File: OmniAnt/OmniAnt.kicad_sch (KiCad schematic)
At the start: 2 parts, among them J1 Conn_01x01_Pin

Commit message: First commit through KiCad
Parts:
- added BT1: Battery_Cell, symbol Device:Battery_Cell
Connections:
- net GND: now also BT1.2 (-)
- net at J1.1 (Pin_1), R1.1: now also BT1.1 (+)
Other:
- moved on the sheet: J1
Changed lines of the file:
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@@
 	(generator_version "9.0")
 	(paper "A4")
-	(wire
-		(pts
-			(xy 110.49 92.71) (xy 110.49 100.33)
+	(junction
+		(at 85.09 82.55)
+		(diameter 0)
+		(color 0 0 0 0)
+	)
+	(junction
+		(at 92.71 82.55)
+		(diameter 0)
+		(color 0 0 0 0)
+	)
+	(junction
+		(at 110.49 92.71)
+		(diameter 0)
+		(color 0 0 0 0)
+	)
+	(wire
+		(pts
+			(xy 92.71 91.44) (xy 92.71 92.71)
+		)
+		(stroke
+			(width 0)
+			(type default)
+		)
+	)
+	(wire
+		(pts
+			(xy 85.09 82.55) (xy 92.71 82.55)
+		)
+		(stroke
+			(width 0)
+			(type default)
+		)
+	)
+	(wire
+		(pts
+			(xy 82.55 82.55) (xy 85.09 82.55)
+		)
+		(stroke
+			(width 0)
+			(type default)
+		)
+	)
+	(wire
+		(pts
+			(xy 92.71 92.71) (xy 110.49 92.71)
+		)
+		(stroke
+			(width 0)
+			(type default)
+		)
+	)
+	(wire
+		(pts
+			(xy 92.71 83.82) (xy 92.71 82.55)
 		)
 		(stroke
@@
 	(wire
 		(pts
-			(xy 95.25 82.55) (xy 110.49 82.55)
-		)
-		(stroke
-			(width 0)
-			(type default)
-		)
-	)
-	(wire
-		(pts
-			(xy 110.49 100.33) (xy 111.76 100.33)
+			(xy 92.71 82.55) (xy 110.49 82.55)
+		)
+		(stroke
+			(width 0)
+			(type default)
+		)
+	)
+	(wire
+		(pts
+			(xy 110.49 92.71) (xy 110.49 102.87)
 		)
 		(stroke
@@
 	(symbol
 		(lib_id "Connector:Conn_01x01_Pin")
-		(at 90.17 82.55 0)
+		(at 80.01 82.55 0)
+		(unit 1)
+		(exclude_from_sim no)
+		(in_bom yes)
+		(on_board yes)
+		(dnp no)
+		(property "Reference" "J1"
+			(at 80.645 77.47 0)
+			(effects
+				(font
+					(size 1.27 1.27)
+				)
+			)
+		)
+		(property "Value" "Conn_01x01_Pin"
+			(at 79.502 76.454 0)
+			(effects
+				(font
+					(size 1.27 1.27)
+				)
+			)
+		)
+		(property "Footprint" ""
+			(at 80.01 82.55 0)
+			(effects
+				(font
+					(size 1.27 1.27)
+				)
+				(hide yes)
+			)
+		)
+		(property "Datasheet" "~"
+			(at 80.01 82.55 0)
+			(effects
+				(font
+					(size 1.27 1.27)
+				)
+				(hide yes)
+			)
+		)
+		(property "Description" "Generic connector, single row, 01x01, script generated"
+			(at 80.01 82.55 0)
+			(effects
+				(font
+					(size 1.27 1.27)
+				)
+				(hide yes)
+			)
+		)
+		(pin "1"
+		)
+		(instances
+			(project ""
+				(path "/af956454-8f11-4118-89f4-dd7ed925536a"
+					(reference "J1")
+					(unit 1)
+				)
+			)
+		)
+	)
+	(symbol
+		(lib_id "Device:Battery_Cell")
+		(at 92.71 88.9 0)
 		(unit 1)
 		(exclude_from_sim no)
@@
 		(dnp no)
 		(fields_autoplaced yes)
-		(property "Reference" "J1"
-			(at 90.805 77.47 0)
-			(effects
-				(font
-					(size 1.27 1.27)
-				)
-			)
-		)
-		(property "Value" "Conn_01x01_Pin"
-			(at 90.805 80.01 0)
-			(effects
-				(font
-					(size 1.27 1.27)
-				)
+		(property "Reference" "BT1"
+			(at 96.52 85.7884 0)
+			(effects
+				(font
+					(size 1.27 1.27)
+				)
+				(justify left)
+			)
+		)
+		(property "Value" "Battery_Cell"
+			(at 96.52 88.3284 0)
+			(effects
+				(font
+					(size 1.27 1.27)
+				)
+				(justify left)
 			)
 		)
 		(property "Footprint" ""
-			(at 90.17 82.55 0)
+			(at 92.71 87.376 90)
 			(effects
 				(font
@@
 		)
 		(property "Datasheet" "~"
-			(at 90.17 82.55 0)
-			(effects
-				(font
-					(size 1.27 1.27)
-				)
-				(hide yes)
-			)
-		)
-		(property "Description" "Generic connector, single row, 01x01, script generated"
-			(at 90.17 82.55 0)
-			(effects
-				(font
-					(size 1.27 1.27)
-				)
-				(hide yes)
-			)
+			(at 92.71 87.376 90)
+			(effects
+				(font
+					(size 1.27 1.27)
+				)
+				(hide yes)
+			)
+		)
+		(property "Description" "Single-cell battery"
+			(at 92.71 88.9 0)
+			(effects
+				(font
+					(size 1.27 1.27)
+				)
+				(hide yes)
+			)
+		)
+		(pin "2"
 		)
 		(pin "1"
@@
 			(project ""
 				(path "/af956454-8f11-4118-89f4-dd7ed925536a"
-					(reference "J1")
+					(reference "BT1")
 					(unit 1)
 				)
@@
 	(symbol
 		(lib_id "power:GND")
-		(at 111.76 100.33 0)
+		(at 110.49 102.87 0)
 		(unit 1)
 		(exclude_from_sim no)
@@
 		(fields_autoplaced yes)
 		(property "Reference" "#PWR01"
-			(at 111.76 106.68 0)
+			(at 110.49 109.22 0)
 			(effects
 				(font
@@
 		)
 		(property "Value" "GND"
-			(at 111.76 105.41 0)
+			(at 110.49 107.95 0)
 			(effects
 				(font
@@
 		)
 		(property "Footprint" ""
-			(at 111.76 100.33 0)
+			(at 110.49 102.87 0)
 			(effects
 				(font
@@
 		)
 		(property "Datasheet" ""
-			(at 111.76 100.33 0)
+			(at 110.49 102.87 0)
 			(effects
 				(font
@@
 		)
 		(property "Description" "Power symbol creates a global label with name \"GND\" , ground"
-			(at 111.76 100.33 0)
-			(effects
-				(font
+			(at 110.49 102.87 0)
+			(effects
+				(font

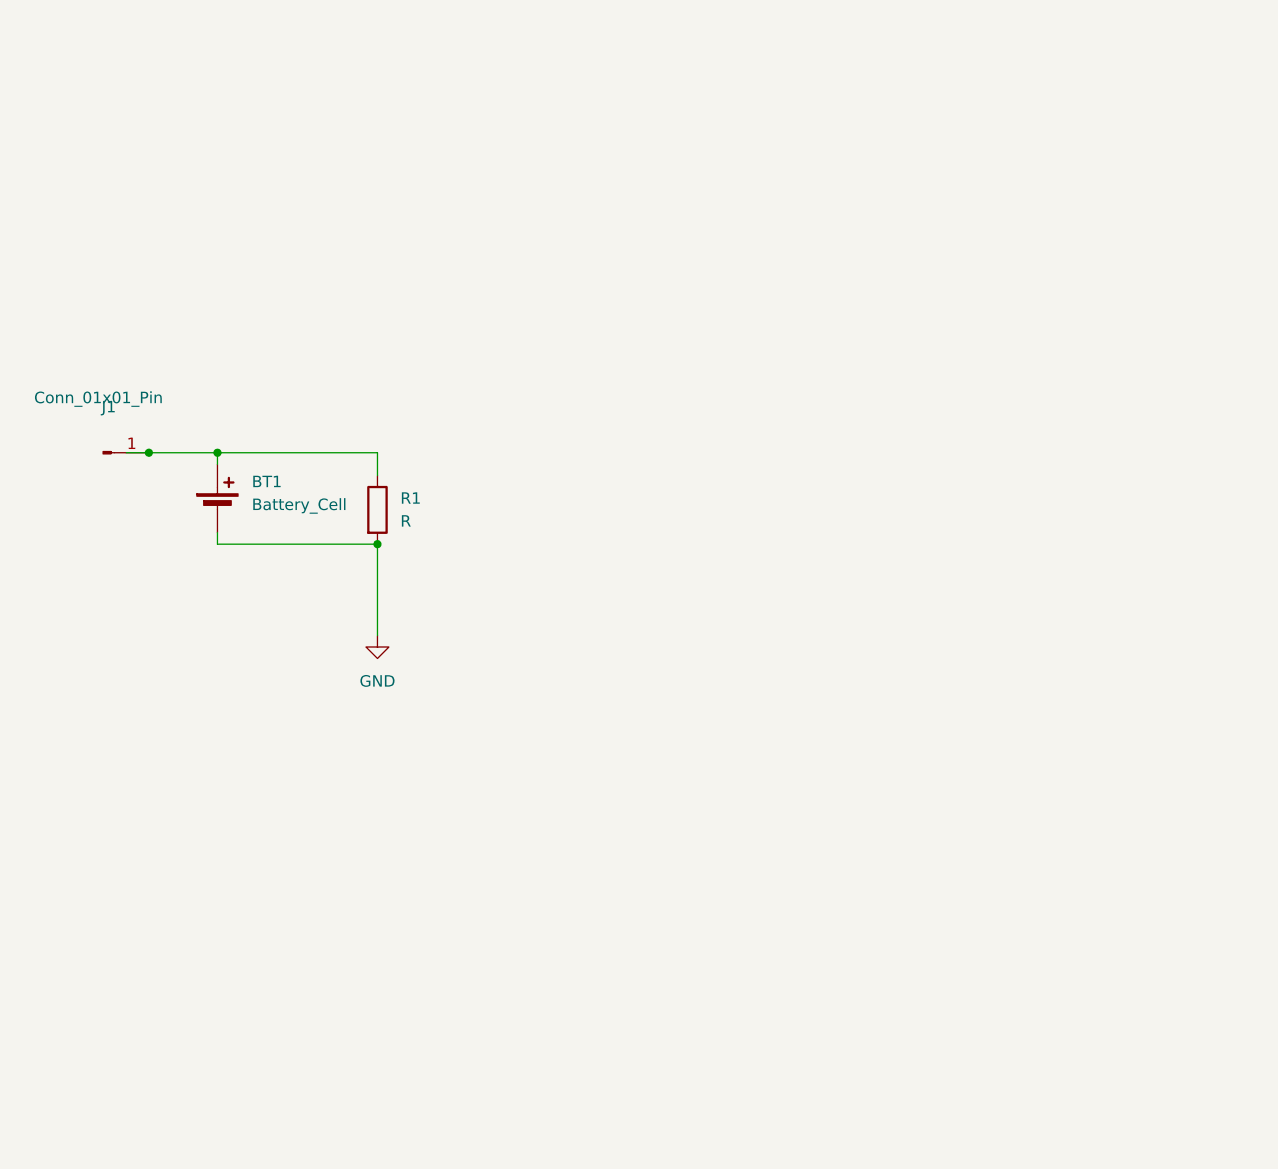
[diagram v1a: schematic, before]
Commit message: I dropped in the esp, DCDC, diode, and usb connector.
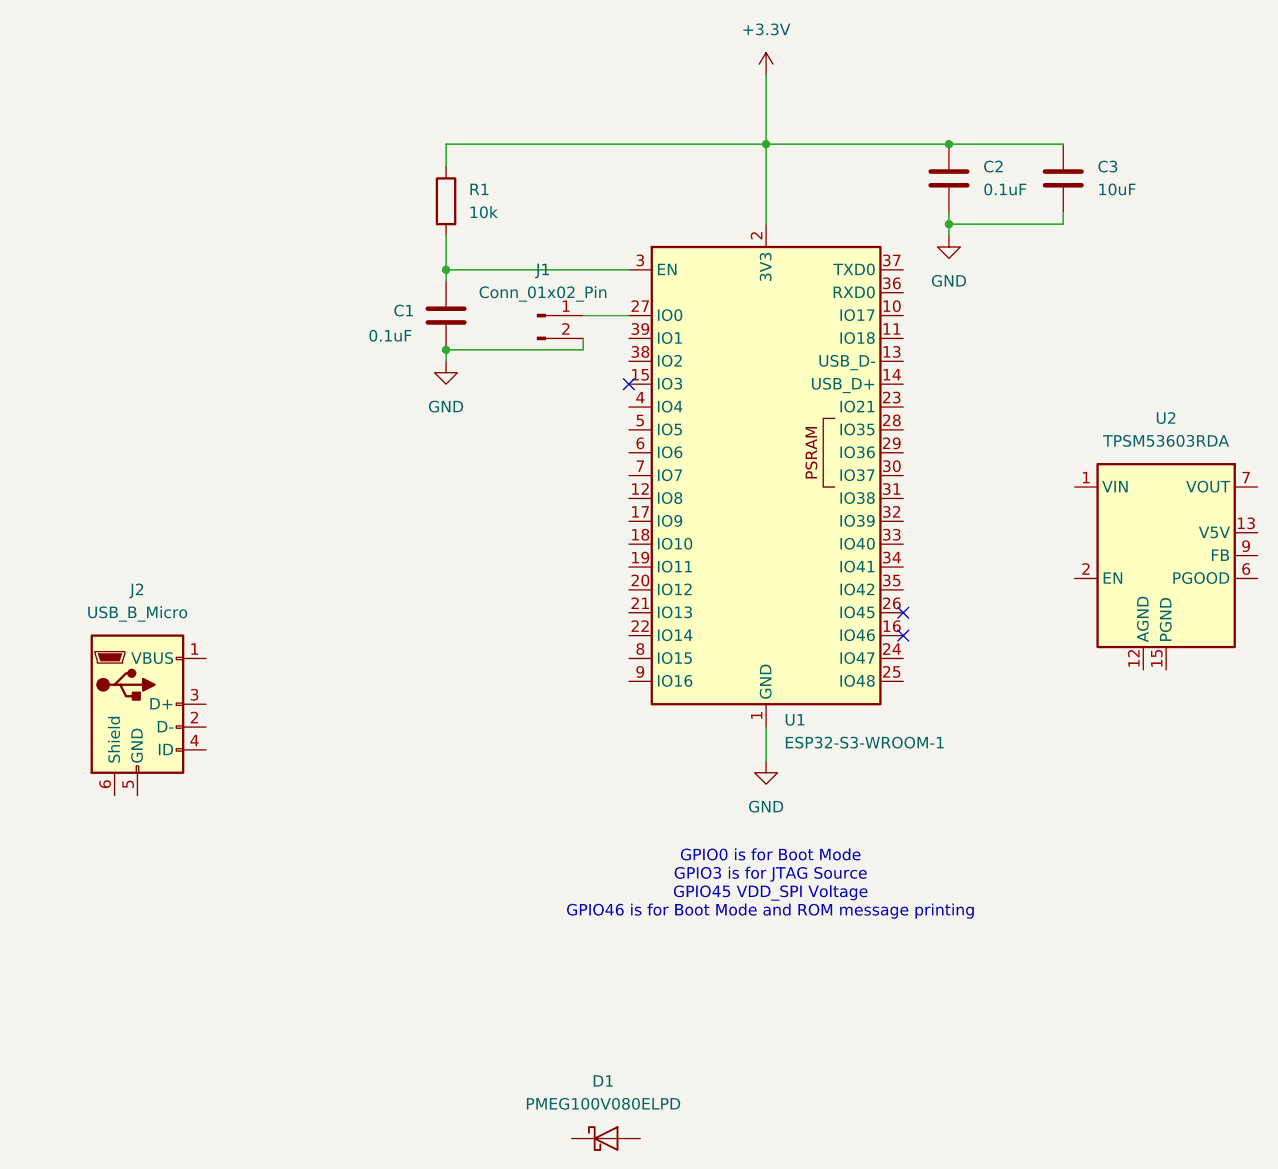
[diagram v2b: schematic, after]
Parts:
- removed BT1: Battery_Cell, symbol Device:Battery_Cell
- removed J1: Conn_01x01_Pin, symbol Connector:Conn_01x01_Pin
- added C1, C2: 0.1uF, Capacitor_SMD:C_0805_2012Metric, symbol Device:C
- added C3: 10uF, Capacitor_SMD:C_0805_2012Metric, symbol Device:C
- added D1: PMEG100V080ELPD, Package_TO_SOT_SMD:Nexperia_CFP15_SOT-1289, symbol Diode:PMEG100V080ELPD
- added J1: Conn_01x02_Pin, Connector_PinHeader_1.27mm:PinHeader_1x02_P1.27mm_Vertical, symbol Connector:Conn_01x02_Pin
- added J2: USB_B_Micro, symbol Connector:USB_B_Micro
- added U1: ESP32-S3-WROOM-1, RF_Module:ESP32-S3-WROOM-1, symbol RF_Module:ESP32-S3-WROOM-1
- added U2: TPSM53603RDA, Package_DFN_QFN:Texas_B3QFN-14-1EP_5x5.5mm_P0.65mm_ThermalVia, symbol Converter_DCDC:TPSM53603RDA
- R1: value R -> 10k; footprint (none) -> Resistor_SMD:R_0805_2012Metric
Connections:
- net GND: now also C1.2, C2.2, C3.2, J1.2 (Pin_2), U1.1 (GND), U1.40 (GND), U1.41 (GND); no longer R1.2
- net +3.3V: now reaches R1.1
- net +3.3V: now also C2.1, C3.1, U1.2 (3V3)
- new net: D1.1 (A), D1.2 (A)
- new net: C1.1, R1.2, U1.3 (EN)
- new net: U2.1 (VIN), U2.14 (VIN)
- new net: U2.10 (PGND), U2.11 (PGND), U2.15 (PGND), U2.3 (PGND)
- new net: U2.7 (VOUT), U2.8 (VOUT)
- new net: J1.1 (Pin_1), U1.27 (IO0)
- no-connect marks 0 -> 3
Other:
- note added: "GPIO0 is for Boot Mode GPIO3 is for JTAG Source GPIO45 VDD_SPI Voltage GPIO46 is for Boot Mode and ROM message printing"

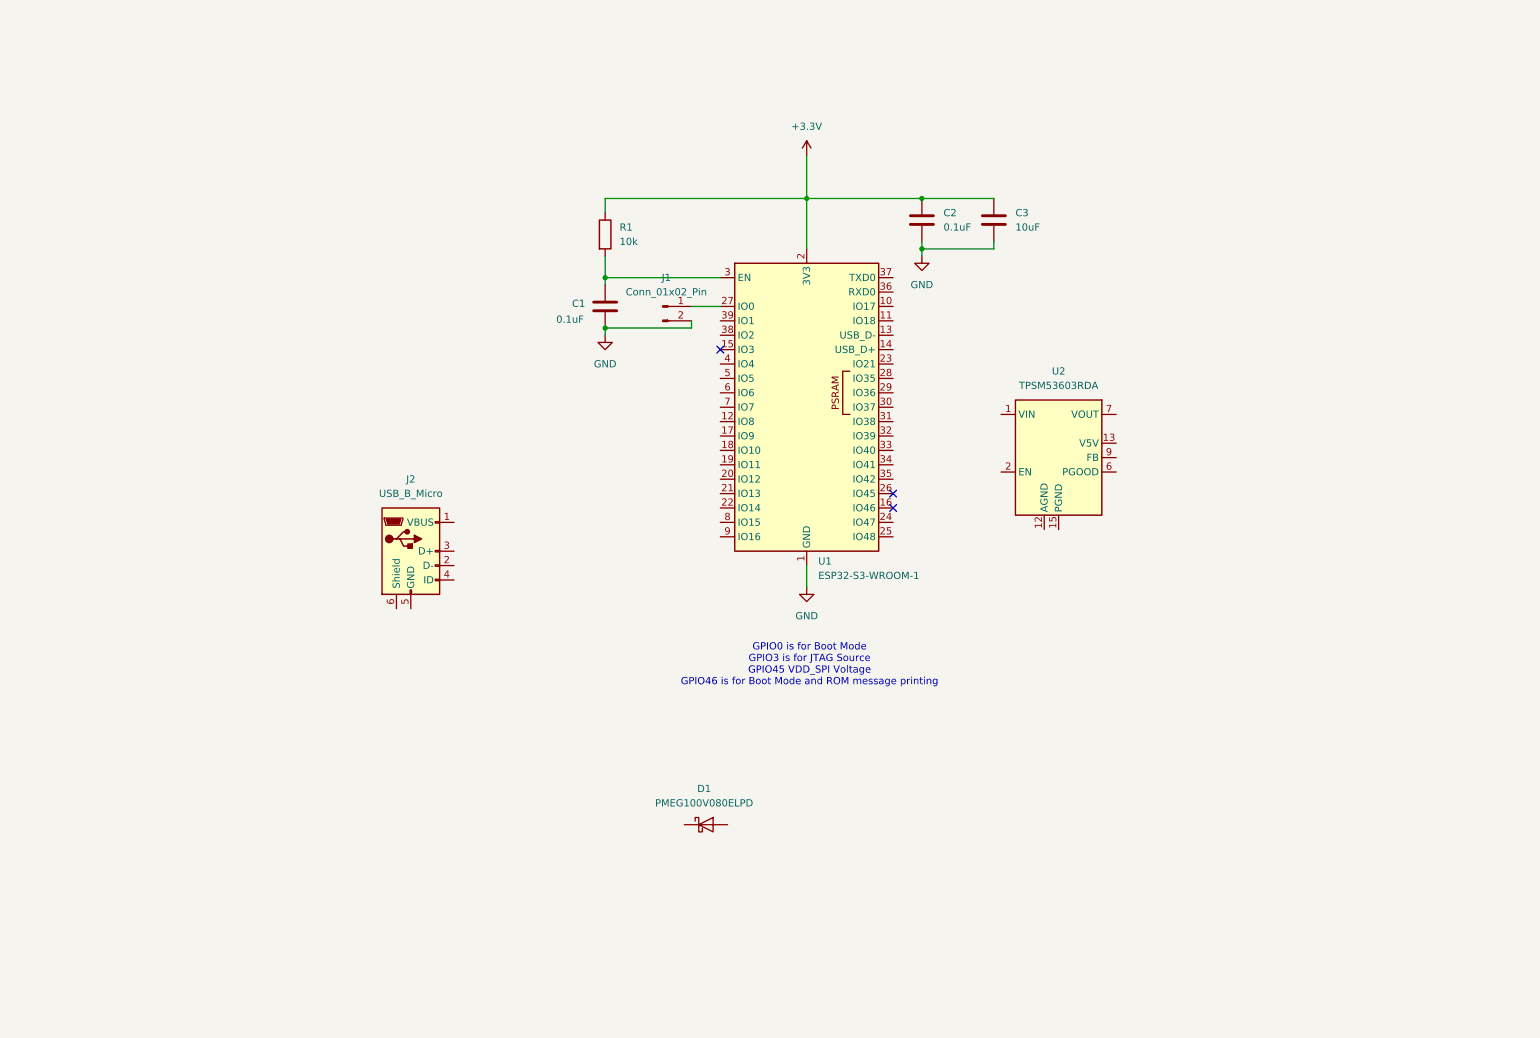
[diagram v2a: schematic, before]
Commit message: Added a schematic for the motor controller.
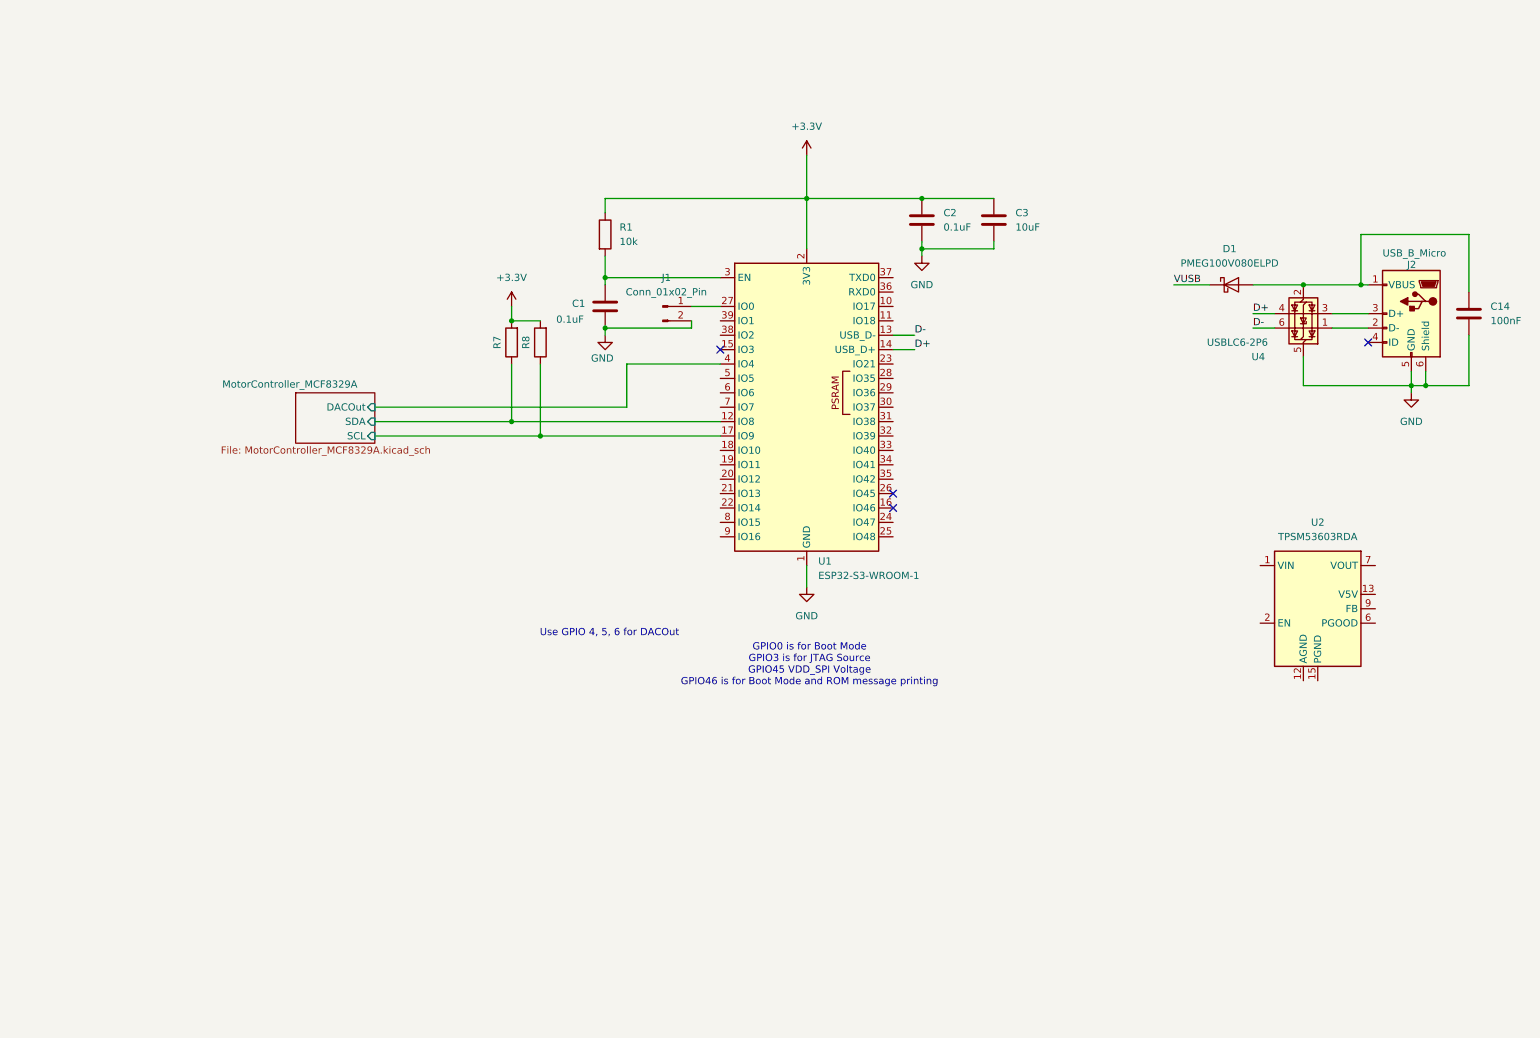
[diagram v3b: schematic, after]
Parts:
- added C14: 100nF, Capacitor_SMD:C_0805_2012Metric, symbol Device:C
- added R7, R8: 5.1k, Resistor_SMD:R_0805_2012Metric, symbol Device:R
- added U4: USBLC6-2P6, Package_TO_SOT_SMD:SOT-666, symbol Power_Protection:USBLC6-2P6
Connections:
- net +3.3V: now also R7.2, R8.2
- net GND: now also J2.5 (GND), J2.6 (Shield), C14.2, U4.5 (VBUS)
- net at D1.1 (A), D1.2 (A): now also J2.1 (VBUS), C14.1, U4.2 (GND)
- net VUSB: now reaches D1.3 (K)
- net at J2.2 (D-): now also U4.1 (I/O1)
- net at J2.3 (D+): now also U4.3 (I/O2)
- net MotorController_MCF8329A/SDA: now reaches U1.12 (IO8)
- net MotorController_MCF8329A/SDA: now also R7.1
- net D-: now reaches U1.13 (USB_D-)
- net D-: now also U4.6 (I/O1)
- net D+: now reaches U1.14 (USB_D+)
- net D+: now also U4.4 (I/O2)
- net MotorController_MCF8329A/SCL: now reaches U1.17 (IO9)
- net MotorController_MCF8329A/SCL: now also R8.1
- net MotorController_MCF8329A/DACOut: now reaches U1.4 (IO4)
- no-connect marks 3 -> 4
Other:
- added sheet MotorController_MCF8329A (MotorController_MCF8329A.kicad_sch)
- note added: "Use GPIO 4, 5, 6 for DACOut"
- moved on the sheet: D1, J2, U2

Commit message: Mostly organizing
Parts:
- removed C1, C2: 0.1uF, Capacitor_SMD:C_0805_2012Metric, symbol Device:C
- removed C14: 100nF, Capacitor_SMD:C_0805_2012Metric, symbol Device:C
- removed C3: 10uF, Capacitor_SMD:C_0805_2012Metric, symbol Device:C
- removed R1: 10k, Resistor_SMD:R_0805_2012Metric, symbol Device:R
- removed R7, R8: 5.1k, Resistor_SMD:R_0805_2012Metric, symbol Device:R
- added C15, C22, C23: 100nF, PCM_JLCPCB:C_0603, symbol PCM_JLCPCB-Capacitors:0603,100nF
- added C7: 10uF, PCM_JLCPCB:C_0805, symbol PCM_JLCPCB-Capacitors:0805,10uF,(2)
- added J3: Connector, USB-TYPE-C-16P, PCM_JLCPCB:TYPE-C-SMD_HX-TYPE-C-16PIN, symbol PCM_JLCPCB-Extended:Connector, USB-TYPE-C-16P
- added R1: 10kΩ, PCM_JLCPCB:R_0402, symbol PCM_JLCPCB-Resistors:0402,10kΩ
- added R11, R12: 5.1kΩ, PCM_JLCPCB:R_0402, symbol PCM_JLCPCB-Resistors:0402,5.1kΩ
- U1: LCSC (none) -> C2913197
- U2: LCSC (none) -> C2860943
- U4: LCSC (none) -> C15999
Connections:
- net +3.3V: now also C22.1, C7.1, R1.1, R11.2, R12.2
- net GND: now also C15.2, C22.2, C23.2, C7.2
- net MotorController_MCF8329A/SCL: now also R11.1
- net MotorController_MCF8329A/SDA: now also R12.1
- net at D1.1 (A), D1.2 (A), J2.1 (VBUS)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: now also C23.1
- net at U1.3 (EN): now also C15.1, R1.2
- new net: J3.A12B1 (GND), J3.B12A1 (GND)
- new net: J3.A9B4 (VBUS), J3.B9A4 (VBUS)

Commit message: Good progress on the power stage today.
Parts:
- removed D1: PMEG100V080ELPD, Package_TO_SOT_SMD:Nexperia_CFP15_SOT-1289, symbol Diode:PMEG100V080ELPD
- removed J2: USB_B_Micro, symbol Connector:USB_B_Micro
- added C10, C9: 10uF, PCM_JLCPCB:C_0805, symbol PCM_JLCPCB-Capacitors:0805,10uF,(2)
- added D2: SSL34F, PCM_JLCPCB:D_SMAF, symbol PCM_JLCPCB-Diodes:Schottky,SSL34F
- added R13, R14, R2: 5.1kΩ, PCM_JLCPCB:R_0402, symbol PCM_JLCPCB-Resistors:0402,5.1kΩ
- added R5: 12kΩ, PCM_JLCPCB:R_0402, symbol PCM_JLCPCB-Resistors:0402,12kΩ
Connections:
- net +3.3V: now also U2.7 (VOUT), U2.8 (VOUT), R5.1
- net D+: now also U4.6 (I/O1); no longer U4.4 (I/O2)
- net D-: now also U4.4 (I/O2); no longer U4.6 (I/O1)
- net GND: now also J3.A12B1 (GND), J3.B12A1 (GND), J3.S1 (SHIELD), U2.10 (PGND), U2.11 (PGND), U2.12 (AGND), U2.15 (PGND), U2.3 (PGND), C10.2, C9.2, R13.2, R14.2, R2.2
- net VUSB: now also C23.1, J3.A9B4 (VBUS), J3.B9A4 (VBUS), U4.2 (GND), D2.2
- net at J3.A5 (CC1): now also R14.1
- net at J3.A6 (D+): now also J3.B6 (D+), U4.1 (I/O1)
- net at J3.A7 (D-): now also J3.B7 (D-), U4.3 (I/O2)
- net at J3.B5 (CC2): now also R13.1
- net Batt: now reaches U2.1 (VIN), U2.14 (VIN)
- net Batt: now also U2.2 (EN), C10.1, C9.1, D2.1
- net at U2.9 (FB): now also R2.1, R5.2
- no-connect marks 4 -> 7
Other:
- sheet MotorController_MCF8329A ports: added PWM; removed none
- moved on the sheet: C15, C22, C23, C7, J1, J3, R1, R11, R12, U1, U2, U4
